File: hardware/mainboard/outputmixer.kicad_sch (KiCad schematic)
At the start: 15 parts, among them J10 MIX, J9 EXT, U12 TL074, U8 TL074

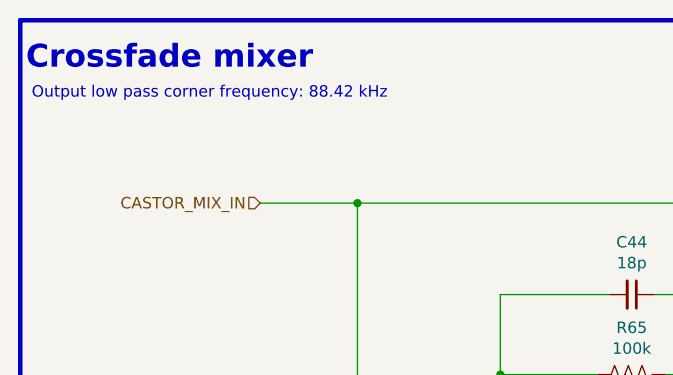
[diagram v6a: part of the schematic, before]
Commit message: Audit BOM, replace some parts with alts
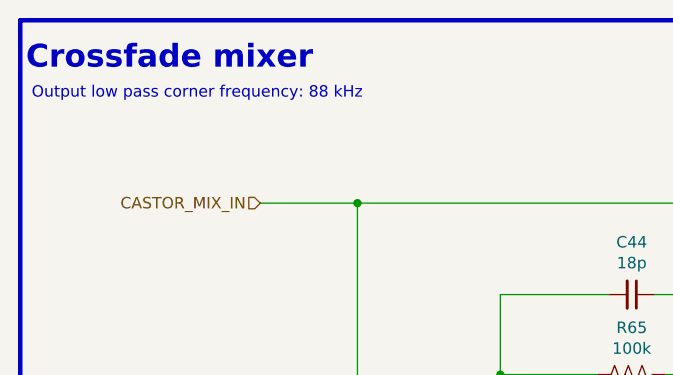
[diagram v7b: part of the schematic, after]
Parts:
- C44, C45: finalized (none) -> yes; mpn (none) -> CL05C180JB5NNNC
- J9: finalized (none) -> NO * UNAVAILABLE *; mpn (none) -> BM08B-GHS-TBT
- R62, R63, R64, R65, R66, R67, R68: Reqs Eurorack level audio, 1%, 2 mW -> Eurorack level audio, 1%, 100 mW, thin film
- R69: Reqs Output impedance, 5%, 150 mW -> Output impedance, 5%, 150 mW, thin film
- RV12: Reqs (none) -> 10k, linear taper, 6.35 mm round shaft, 15 mm height; finalized (none) -> yes; mpn R0904N-???? L-25KQ/LWS -> https://www.thonk.co.uk/shop/vertical-b10k-10k-linear/
- U12, U8: finalized (none) -> yes
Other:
- note added: "Output low pass corner frequency: 88 kHz"
- note removed: "Output low pass corner frequency: 88.42 kHz"
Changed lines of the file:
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@@
     (effects (font (size 2.54 2.54) bold) (justify left bottom))
   )
-  (text "Output low pass corner frequency: 88.42 kHz" (at 55.245 33.02 0)
+  (text "Output low pass corner frequency: 88 kHz" (at 55.245 33.02 0)
     (effects (font (size 1.27 1.27)) (justify left bottom))
   )
@@
       (effects (font (size 1.27 1.27)) hide)
     )
-    (property "Reqs" "Eurorack level audio, 1%, 2 mW" (id 4) (at 99.695 69.85 0)
+    (property "Reqs" "Eurorack level audio, 1%, 100 mW, thin film" (id 4) (at 99.695 69.85 0)
       (effects (font (size 1.27 1.27)) hide)
     )
@@
       (effects (font (size 1.27 1.27)) hide)
     )
-    (property "Reqs" "Eurorack level audio, 1%, 2 mW" (id 4) (at 99.695 74.93 0)
+    (property "Reqs" "Eurorack level audio, 1%, 100 mW, thin film" (id 4) (at 99.695 74.93 0)
       (effects (font (size 1.27 1.27)) hide)
     )
@@
       (effects (font (size 1.27 1.27)) hide)
     )
-    (property "Reqs" "Eurorack level audio, 1%, 2 mW" (id 4) (at 107.315 82.55 0)
+    (property "Reqs" "Eurorack level audio, 1%, 100 mW, thin film" (id 4) (at 107.315 82.55 0)
       (effects (font (size 1.27 1.27)) hide)
     )
@@
       (effects (font (size 1.27 1.27)) hide)
     )
-    (property "Reqs" "Eurorack level audio, 1%, 2 mW" (id 4) (at 121.92 63.5 0)
+    (property "Reqs" "Eurorack level audio, 1%, 100 mW, thin film" (id 4) (at 121.92 63.5 0)
       (effects (font (size 1.27 1.27)) hide)
     )
@@
       (effects (font (size 1.27 1.27)) hide)
     )
-    (property "Reqs" "Eurorack level audio, 1%, 2 mW" (id 4) (at 147.32 44.45 0)
+    (property "Reqs" "Eurorack level audio, 1%, 100 mW, thin film" (id 4) (at 147.32 44.45 0)
       (effects (font (size 1.27 1.27)) hide)
     )
@@
       (effects (font (size 1.27 1.27)) hide)
     )
-    (property "finalized" "" (id 4) (at 121.92 54.61 0)
-      (effects (font (size 1.27 1.27)) hide)
-    )
-    (property "mpn" "" (id 5) (at 121.92 54.61 0)
+    (property "finalized" "yes" (id 4) (at 121.92 54.61 0)
+      (effects (font (size 1.27 1.27)) hide)
+    )
+    (property "mpn" "CL05C180JB5NNNC" (id 5) (at 121.92 54.61 0)
       (effects (font (size 1.27 1.27)) hide)
     )
@@
       (effects (font (size 1.27 1.27)) hide)
     )
-    (property "Reqs" "Eurorack level audio, 1%, 2 mW" (id 4) (at 147.32 82.55 0)
+    (property "Reqs" "Eurorack level audio, 1%, 100 mW, thin film" (id 4) (at 147.32 82.55 0)
       (effects (font (size 1.27 1.27)) hide)
     )
@@
       (effects (font (size 1.27 1.27)) hide)
     )
-    (property "Reqs" "Eurorack level audio, 1%, 2 mW" (id 4) (at 173.99 76.2 0)
+    (property "Reqs" "Eurorack level audio, 1%, 100 mW, thin film" (id 4) (at 173.99 76.2 0)
       (effects (font (size 1.27 1.27)) hide)
     )
@@
       (effects (font (size 1.27 1.27)) hide)
     )
-    (property "Reqs" "Output impedance, 5%, 150 mW" (id 4) (at 189.23 85.09 0)
+    (property "Reqs" "Output impedance, 5%, 150 mW, thin film" (id 4) (at 189.23 85.09 0)
       (effects (font (size 1.27 1.27)) hide)
     )
@@
       (effects (font (size 1.27 1.27)) hide)
     )
-    (property "finalized" "" (id 4) (at 173.99 67.31 0)
-      (effects (font (size 1.27 1.27)) hide)
-    )
-    (property "mpn" "" (id 5) (at 173.99 67.31 0)
+    (property "finalized" "yes" (id 4) (at 173.99 67.31 0)
+      (effects (font (size 1.27 1.27)) hide)
+    )
+    (property "mpn" "CL05C180JB5NNNC" (id 5) (at 173.99 67.31 0)
       (effects (font (size 1.27 1.27)) hide)
     )
@@
     )
     (property "Datasheet" "~" (id 3) (at 157.48 142.24 0)
+      (effects (font (size 1.27 1.27)) hide)
+    )
+    (property "finalized" "NO * UNAVAILABLE *" (id 4) (at 157.48 142.24 0)
+      (effects (font (size 1.27 1.27)) hide)
+    )
+    (property "mpn" "BM08B-GHS-TBT" (id 5) (at 157.48 142.24 0)
       (effects (font (size 1.27 1.27)) hide)
     )
@@
     )
     (property "mpn" "TL074CPW" (id 5) (at 173.99 92.71 0)
+      (effects (font (size 1.27 1.27)) hide)
+    )
+    (property "finalized" "yes" (id 6) (at 173.99 85.09 0)
       (effects (font (size 1.27 1.27)) hide)
     )
@@
       (effects (font (size 1.27 1.27)) hide)
     )
-    (property "mpn" "R0904N-???? L-25KQ/LWS" (id 4) (at 147.32 82.55 0)
+    (property "mpn" "https://www.thonk.co.uk/shop/vertical-b10k-10k-linear/" (id 4) (at 147.32 82.55 0)
+      (effects (font (size 1.27 1.27)) hide)
+    )
+    (property "Reqs" "10k, linear taper, 6.35 mm round shaft, 15 mm height" (id 5) (at 133.35 82.55 0)
+      (effects (font (size 1.27 1.27)) hide)
+    )
+    (property "finalized" "yes" (id 6) (at 133.35 82.55 0)
       (effects (font (size 1.27 1.27)) hide)
     )
@@
       (effects (font (size 1.27 1.27)) hide)
     )
+    (property "finalized" "yes" (id 6) (at 114.935 72.39 0)
+      (effects (font (size 1.27 1.27)) hide)
+    )

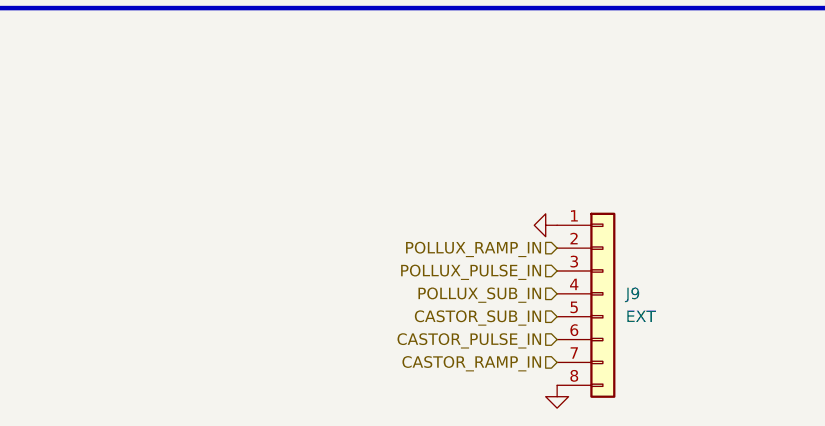
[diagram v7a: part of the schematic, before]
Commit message: Switch EXT header to a 2x5 1.27mm pitch IDC header
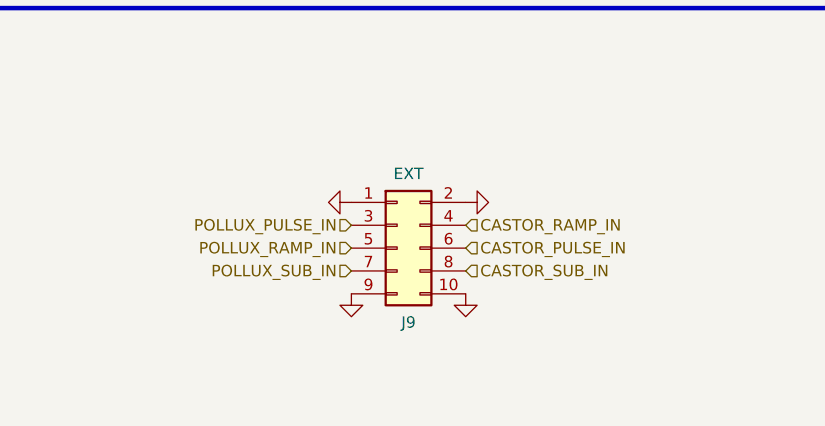
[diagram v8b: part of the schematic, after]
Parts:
- removed J9: EXT, Connector_JST:JST_GH_BM08B-GHS-TBT_1x08-1MP_P1.25mm_Vertical, symbol Connector_Generic:Conn_01x08
- added J9: EXT, winterbloom:Connector_Cortex_Debug_IDC_2x05_P1.27mm_Vertical_Shrouded_SMD, symbol Connector_Generic:Conn_02x05_Odd_Even
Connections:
- net CASTOR_PULSE_IN: now also J9.6 (Pin_6)
- net CASTOR_RAMP_IN: now also J9.4 (Pin_4)
- net CASTOR_SUB_IN: now also J9.8 (Pin_8)
- net GND: now also J9.1 (Pin_1), J9.10 (Pin_10), J9.2 (Pin_2), J9.9 (Pin_9)
- net POLLUX_PULSE_IN: now also J9.3 (Pin_3)
- net POLLUX_RAMP_IN: now also J9.5 (Pin_5)
- net POLLUX_SUB_IN: now also J9.7 (Pin_7)
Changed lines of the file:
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@@
     (effects (font (size 1.27 1.27)) (justify left bottom))
   )
-  (hierarchical_label "POLLUX_RAMP_IN" (shape input) (at 152.4 137.16 180)
+  (hierarchical_label "POLLUX_RAMP_IN" (shape input) (at 129.54 137.16 180)
     (effects (font (size 1.27 1.27)) (justify right))
   )
-  (hierarchical_label "CASTOR_RAMP_IN" (shape input) (at 152.4 149.86 180)
-    (effects (font (size 1.27 1.27)) (justify right))
+  (hierarchical_label "CASTOR_RAMP_IN" (shape input) (at 142.24 134.62 0)
+    (effects (font (size 1.27 1.27)) (justify left))
   )
   (hierarchical_label "POLLUX_MIX_IN" (shape input) (at 80.645 74.93 180)
     (effects (font (size 1.27 1.27)) (justify right))
   )
-  (hierarchical_label "CASTOR_PULSE_IN" (shape input) (at 152.4 147.32 180)
+  (hierarchical_label "CASTOR_PULSE_IN" (shape input) (at 142.24 137.16 0)
+    (effects (font (size 1.27 1.27)) (justify left))
+  )
+  (hierarchical_label "POLLUX_PULSE_IN" (shape input) (at 129.54 134.62 180)
     (effects (font (size 1.27 1.27)) (justify right))
   )
-  (hierarchical_label "POLLUX_PULSE_IN" (shape input) (at 152.4 139.7 180)
-    (effects (font (size 1.27 1.27)) (justify right))
-  )
-  (hierarchical_label "POLLUX_SUB_IN" (shape input) (at 152.4 142.24 180)
+  (hierarchical_label "POLLUX_SUB_IN" (shape input) (at 129.54 139.7 180)
     (effects (font (size 1.27 1.27)) (justify right))
   )
@@
     (effects (font (size 1.27 1.27)) (justify right))
   )
-  (hierarchical_label "CASTOR_SUB_IN" (shape input) (at 152.4 144.78 180)
-    (effects (font (size 1.27 1.27)) (justify right))
+  (hierarchical_label "CASTOR_SUB_IN" (shape input) (at 142.24 139.7 0)
+    (effects (font (size 1.27 1.27)) (justify left))
   )
   (symbol (lib_id "Device:R_US") (at 99.695 69.85 270) (unit 1)
@@
     (pin "2")
   )
-  (symbol (lib_id "Connector_Generic:Conn_01x08") (at 157.48 142.24 0) (unit 1)
+  (symbol (lib_id "power:GND") (at 142.24 132.08 90) (unit 1)
     (in_bom yes) (on_board yes) (fields_autoplaced)
-    (property "Reference" "J9" (id 0) (at 160.02 142.2399 0)
-      (effects (font (size 1.27 1.27)) (justify left))
-    )
-    (property "Value" "EXT" (id 1) (at 160.02 144.7799 0)
-      (effects (font (size 1.27 1.27)) (justify left))
-    )
-    (property "Footprint" "Connector_JST:JST_GH_BM08B-GHS-TBT_1x08-1MP_P1.25mm_Vertical" (id 2) (at 157.48 142.24 0)
-      (effects (font (size 1.27 1.27)) hide)
-    )
-    (property "Datasheet" "~" (id 3) (at 157.48 142.24 0)
-      (effects (font (size 1.27 1.27)) hide)
-    )
-    (property "finalized" "NO * UNAVAILABLE *" (id 4) (at 157.48 142.24 0)
-      (effects (font (size 1.27 1.27)) hide)
-    )
-    (property "mpn" "BM08B-GHS-TBT" (id 5) (at 157.48 142.24 0)
-      (effects (font (size 1.27 1.27)) hide)
-    )
-    (pin "1")
-    (pin "2")
-    (pin "3")
-    (pin "4")
-    (pin "5")
-    (pin "6")
-    (pin "7")
-    (pin "8")
-  )
-  (symbol (lib_id "power:GND") (at 152.4 152.4 0) (unit 1)
-    (in_bom yes) (on_board yes) (fields_autoplaced)
-    (property "Reference" "#PWR092" (id 0) (at 152.4 158.75 0)
-      (effects (font (size 1.27 1.27)) hide)
-    )
-    (property "Value" "GND" (id 1) (at 152.4 156.845 0)
-      (effects (font (size 1.27 1.27)) hide)
-    )
-    (property "Footprint" "" (id 2) (at 152.4 152.4 0)
-      (effects (font (size 1.27 1.27)) hide)
-    )
-    (property "Datasheet" "" (id 3) (at 152.4 152.4 0)
+    (property "Reference" "#PWR0104" (id 0) (at 148.59 132.08 0)
+      (effects (font (size 1.27 1.27)) hide)
+    )
+    (property "Value" "GND" (id 1) (at 146.685 132.08 0)
+      (effects (font (size 1.27 1.27)) hide)
+    )
+    (property "Footprint" "" (id 2) (at 142.24 132.08 0)
+      (effects (font (size 1.27 1.27)) hide)
+    )
+    (property "Datasheet" "" (id 3) (at 142.24 132.08 0)
       (effects (font (size 1.27 1.27)) hide)
     )
@@
     (pin "4")
   )
+  (symbol (lib_id "Connector_Generic:Conn_02x05_Odd_Even") (at 134.62 137.16 0) (unit 1)
+    (in_bom yes) (on_board yes)
+    (property "Reference" "J9" (id 0) (at 135.89 145.415 0))
+    (property "Value" "EXT" (id 1) (at 135.89 128.905 0))
+    (property "Footprint" "winterbloom:Connector_Cortex_Debug_IDC_2x05_P1.27mm_Vertical_Shrouded_SMD" (id 2) (at 134.62 137.16 0)
+      (effects (font (size 1.27 1.27)) hide)
+    )
+    (property "Datasheet" "https://www.cnctech.us/pdfs/3220-XX-0300-00_.pdf" (id 3) (at 134.62 137.16 0)
+      (effects (font (size 1.27 1.27)) hide)
+    )
+    (property "mpn" "3220-10-0300-00" (id 4) (at 134.62 137.16 0)
+      (effects (font (size 1.27 1.27)) hide)
+    )
+    (property "finalized" "yes" (id 5) (at 134.62 137.16 0)
+      (effects (font (size 1.27 1.27)) hide)
+    )
+    (pin "1")
+    (pin "10")
+    (pin "2")
+    (pin "3")
+    (pin "4")
+    (pin "5")
+    (pin "6")
+    (pin "7")
+    (pin "8")
+    (pin "9")
+  )
+  (symbol (lib_id "power:GND") (at 129.54 142.24 0) (unit 1)
+    (in_bom yes) (on_board yes) (fields_autoplaced)
+    (property "Reference" "#PWR0102" (id 0) (at 129.54 148.59 0)
+      (effects (font (size 1.27 1.27)) hide)
+    )
+    (property "Value" "GND" (id 1) (at 129.54 146.685 0)
+      (effects (font (size 1.27 1.27)) hide)
+    )
+    (property "Footprint" "" (id 2) (at 129.54 142.24 0)
+      (effects (font (size 1.27 1.27)) hide)
+    )
+    (property "Datasheet" "" (id 3) (at 129.54 142.24 0)
+      (effects (font (size 1.27 1.27)) hide)
+    )
+    (pin "1")
+  )
   (symbol (lib_id "winterbloom:Eurorack_Mono_Jack") (at 203.2 83.82 0) (unit 1)
     (in_bom yes) (on_board yes)
@@
     (pin "2")
     (pin "3")
+  )
+  (symbol (lib_id "power:GND") (at 142.24 142.24 0) (unit 1)
+    (in_bom yes) (on_board yes) (fields_autoplaced)
+    (property "Reference" "#PWR0103" (id 0) (at 142.24 148.59 0)
+      (effects (font (size 1.27 1.27)) hide)
+    )
+    (property "Value" "GND" (id 1) (at 142.24 146.685 0)
+      (effects (font (size 1.27 1.27)) hide)
+    )
+    (property "Footprint" "" (id 2) (at 142.24 142.24 0)
+      (effects (font (size 1.27 1.27)) hide)
+    )
+    (property "Datasheet" "" (id 3) (at 142.24 142.24 0)
+      (effects (font (size 1.27 1.27)) hide)
+    )
+    (pin "1")
   )
   (symbol (lib_id "winterbloom:TL074") (at 114.935 72.39 0) (mirror x) (unit 3)
@@
     (pin "4")
   )
-  (symbol (lib_id "power:GND") (at 152.4 134.62 270) (unit 1)
+  (symbol (lib_id "power:GND") (at 129.54 132.08 270) (unit 1)
     (in_bom yes) (on_board yes) (fields_autoplaced)
-    (property "Reference" "#PWR091" (id 0) (at 146.05 134.62 0)
-      (effects (font (size 1.27 1.27)) hide)
-    )
-    (property "Value" "GND" (id 1) (at 147.955 134.62 0)
-      (effects (font (size 1.27 1.27)) hide)
-    )
-    (property "Footprint" "" (id 2) (at 152.4 134.62 0)
-      (effects (font (size 1.27 1.27)) hide)
-    )
-    (property "Datasheet" "" (id 3) (at 152.4 134.62 0)
-      (effects (font (size 1.27 1.27)) hide)
-    )
+    (property "Reference" "#PWR091" (id 0) (at 123.19 132.08 0)
+      (effects (font (size 1.27 1.27)) hide)
+    )
+    (property "Value" "GND" (id 1) (at 125.095 132.08 0)
+      (effects (font (size 1.27 1.27)) hide)
+    )
+    (property "Footprint" "" (id 2) (at 129.54 132.08 0)
+      (effects (font (size 1.27 1.27)) hide)
+    )
+    (property "Datasheet" "" (id 3) (at 129.54 132.08 0)
+      (effects (font (size 1.27 1.27)) hide)
+    )
